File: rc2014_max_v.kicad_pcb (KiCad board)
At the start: 2 copper layers, 101.6 x 50.8 mm, 105 parts, among them J1 M3 Mounting Hole, J2 Conn_01x40, J3 Pro Bus, J4 Conn_01x24, J5 AVR-JTAG-10, J6 USB_B_Micro, J7 PMOD, J8 PMOD, SW1 SW_Push, SW2 SW_Push, U1 MIC5356-SGYMME, U10 93LCxxBxxOT, U11 5M570ZT100I5N, U12 IS61LV5128AL-10TLI, U2 SN74ALVC164245DGG, U3 SN74ALVC164245DGG, U4 TXB0108PWR, U5 TXB0108PWR, U6 SN74ALVC164245DGG, U7 MIC5356-SGYMME, U8 TPD2EUSB30, U9 FT2232H, X1 CB3LV-3I-50M0000, Y1 CTS-445 12Mhz

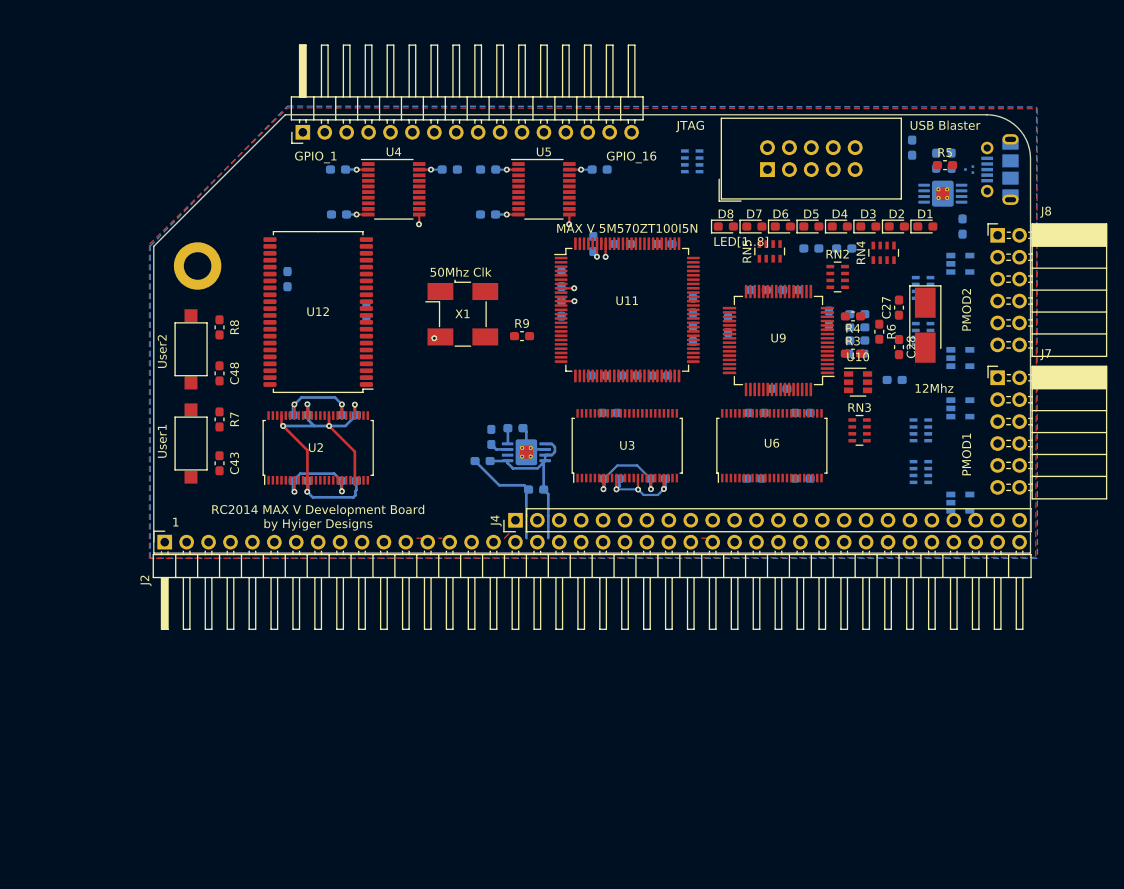
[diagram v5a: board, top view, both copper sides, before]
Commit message: Added logo, cpio vcc selection
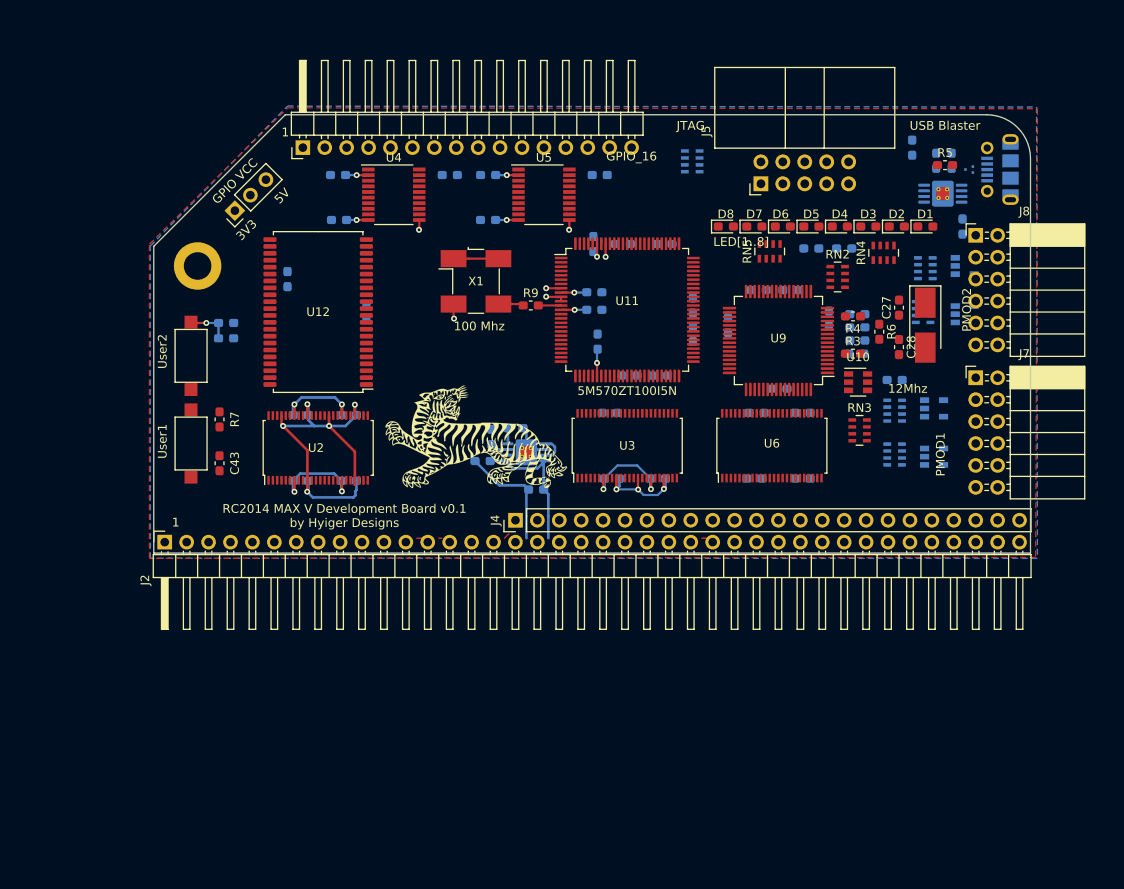
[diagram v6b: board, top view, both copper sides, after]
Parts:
- added G***: LOGO, Logos:asian_tiger, F.Cu at (112.8, 114.0)
- added JP1: Jumper_3_Bridged12, Connector_PinHeader_2.54mm:PinHeader_1x03_P2.54mm_Vertical, F.Cu at (84.8, 87.8)
- C48, R8: moved to B.Cu
- J5: footprint Connector_IDC:IDC-Header_2x05_P2.54mm_Vertical -> Connector_IDC:IDC-Header_2x05_P2.54mm_Horizontal
- moved D11 6.14 mm to (165.9, 116.3)
- moved C48 5.89 mm to (83.8, 100.8), turned to 0 degrees
- moved D9 5.11 mm to (169.4, 99.8)
- moved C41 4.10 mm to (126.5, 97.3), turned to 0 degrees
- moved X1 4.10 mm to (112.8, 96.0)
- moved C40 3.94 mm to (126.9, 103.0), turned to 90 degrees
- moved C47 3.81 mm to (126.5, 99.3), turned to 0 degrees
- moved RN9 3.81 mm to (161.3, 111.0)
- moved R9 3.70 mm to (119.1, 98.8)
- moved RN8 3.66 mm to (161.3, 116.1)
- moved D12 3.05 mm to (165.9, 110.7)
- moved J7 2.54 mm to (170.7, 107.2)
- moved J8 2.54 mm to (170.7, 90.7)
- moved RN6 2.54 mm to (164.6, 99.6)
- moved RN7 2.30 mm to (164.8, 94.5)
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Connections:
- C16 pad 1: 5V -> VCC_GPIO
- C17 pad 1: 5V -> VCC_GPIO
- D1 pad 1: LED1 -> (no net)
- D2 pad 1: LED2 -> (no net)
- D3 pad 1: LED3 -> (no net)
- D4 pad 1: LED4 -> (no net)
- D5 pad 1: LED5 -> (no net)
- D6 pad 1: LED6 -> (no net)
- D7 pad 1: LED7 -> (no net)
- D8 pad 1: LED8 -> (no net)
- J2 pad 35: TX_A -> (no net)
- J2 pad 37: Net-(J2-Pad37) -> (no net)
- J2 pad 38: Net-(J2-Pad38) -> (no net)
- J2 pad 39: Net-(J2-Pad39) -> (no net)
- J2 pad 40: Net-(J2-Pad40) -> (no net)
- J4 pad 19: TX_B -> (no net)
- J4 pad 20: RX_B -> (no net)
- J4 pad 21: Net-(J4-Pad21) -> (no net)
- J4 pad 22: Net-(J4-Pad22) -> (no net)
- J4 pad 23: Net-(J4-Pad23) -> (no net)
- J4 pad 24: Net-(J4-Pad24) -> (no net)
- J4 pad 3: ~RFSH -> (no net)
- J4 pad 5: CLK2 -> (no net)
- J5 pad 4: Net-(J5-Pad4) -> +3V3
- J5 pad 6: Net-(J5-Pad6) -> +3V3
- J5 pad 7: Net-(J5-Pad7) -> (no net)
- J5 pad 8: Net-(J5-Pad8) -> (no net)
- RN1 pad 8: +3V3 -> GND
- RN3 pad 4: Net-(RN3-Pad4) -> (no net)
- U1 pad 6: Net-(U1-Pad6) -> (no net)
- U11 pad 22: Net-(U11-Pad22) -> (no net)
- U11 pad 23: Net-(U11-Pad23) -> (no net)
- U11 pad 24: Net-(U11-Pad24) -> (no net)
- U11 pad 25: Net-(U11-Pad25) -> (no net)
- U11 pad 41: ~M1_F -> D0_F
- U11 pad 42: ~MREQ_F -> D1_F
- U11 pad 43: ~WR_F -> D2_F
- U11 pad 44: ~RD_F -> D3_F
- U11 pad 47: ~IORQ_F -> D4_F
- U11 pad 48: ~PAGE_F -> D5_F
- U11 pad 49: ~BUSACK_F -> D6_F
- U11 pad 50: Net-(U11-Pad50) -> D7_F
- U11 pad 51: Net-(U11-Pad51) -> (no net)
- U11 pad 61: Net-(U11-Pad61) -> ~BUSACK_F
- U11 pad 62: Net-(U11-Pad62) -> ~PAGE_F
- U11 pad 64: Net-(U11-Pad64) -> ~IORQ_F
- U11 pad 66: Net-(U11-Pad66) -> ~RD_F
- U11 pad 67: RX_A_F -> ~WR_F
- U11 pad 68: Net-(U11-Pad68) -> ~MREQ_F
- U11 pad 69: Net-(U11-Pad69) -> ~M1_F
- U11 pad 70: Net-(U11-Pad70) -> (no net)
- U11 pad 71: Net-(U11-Pad71) -> (no net)
- U11 pad 72: Net-(U11-Pad72) -> (no net)
- U11 pad 73: Net-(U11-Pad73) -> (no net)
- U11 pad 74: Net-(U11-Pad74) -> (no net)
- U11 pad 75: Net-(U11-Pad75) -> (no net)
- U11 pad 76: Net-(U11-Pad76) -> (no net)
- U11 pad 77: Net-(U11-Pad77) -> (no net)
- U11 pad 78: Net-(U11-Pad78) -> (no net)
- U12 pad 1: Net-(U12-Pad1) -> (no net)
- U12 pad 15: Net-(U12-Pad15) -> (no net)
- U12 pad 2: Net-(U12-Pad2) -> (no net)
- U12 pad 21: Net-(U12-Pad21) -> (no net)
- U12 pad 22: Net-(U12-Pad22) -> (no net)
- U12 pad 23: Net-(U12-Pad23) -> (no net)
- U12 pad 24: Net-(U12-Pad24) -> (no net)
- U12 pad 25: Net-(U12-Pad25) -> (no net)
- U12 pad 37: Net-(U12-Pad37) -> (no net)
- U12 pad 39: Net-(U12-Pad39) -> (no net)
- U12 pad 40: Net-(U12-Pad40) -> (no net)
- U12 pad 41: Net-(U12-Pad41) -> (no net)
- U12 pad 42: Net-(U12-Pad42) -> (no net)
- U12 pad 43: Net-(U12-Pad43) -> (no net)
- U12 pad 44: Net-(U12-Pad44) -> (no net)
- U12 pad 8: Net-(U12-Pad8) -> (no net)
- U3 pad 25: OE_C_I -> (no net)
- U3 pad 37: RX_A_F -> (no net)
- U3 pad 48: OE_C_O -> (no net)
- U3 pad 5: ~RESET2 -> (no net)
- U4 pad 1: Net-(U4-Pad1) -> (no net)
- U4 pad 19: 5V -> VCC_GPIO
- U4 pad 3: Net-(U4-Pad3) -> (no net)
- U4 pad 4: Net-(U4-Pad4) -> (no net)
- U4 pad 5: Net-(U4-Pad5) -> (no net)
- U4 pad 6: Net-(U4-Pad6) -> (no net)
- U4 pad 7: Net-(U4-Pad7) -> (no net)
- U4 pad 8: Net-(U4-Pad8) -> (no net)
- U4 pad 9: Net-(U4-Pad9) -> (no net)
- U5 pad 1: Net-(U5-Pad1) -> (no net)
- U5 pad 19: 5V -> VCC_GPIO
- U5 pad 3: Net-(U5-Pad3) -> (no net)
- U5 pad 4: Net-(U5-Pad4) -> (no net)
- U5 pad 5: Net-(U5-Pad5) -> (no net)
- U5 pad 6: Net-(U5-Pad6) -> (no net)
- U5 pad 7: Net-(U5-Pad7) -> (no net)
- U5 pad 8: Net-(U5-Pad8) -> (no net)
- U5 pad 9: Net-(U5-Pad9) -> (no net)
- U6 pad 26: D15_F -> (no net)
- U6 pad 29: D14_F -> (no net)
- U6 pad 32: D13_F -> (no net)
- U6 pad 35: D12_F -> (no net)
- U6 pad 37: D11_F -> (no net)
- U6 pad 40: D10_F -> (no net)
- U6 pad 43: D9_F -> (no net)
- U6 pad 46: D8_F -> (no net)
- U7 pad 6: Net-(U7-Pad6) -> (no net)
- U9 pad 21: Net-(U9-Pad21) -> (no net)
- U9 pad 22: Net-(U9-Pad22) -> (no net)
- U9 pad 23: Net-(U9-Pad23) -> (no net)
- U9 pad 24: Net-(U9-Pad24) -> (no net)
- U9 pad 26: Net-(U9-Pad26) -> (no net)
- U9 pad 27: Net-(U9-Pad27) -> (no net)
- U9 pad 28: Net-(U9-Pad28) -> (no net)
- U9 pad 29: Net-(U9-Pad29) -> (no net)
- U9 pad 30: Net-(U9-Pad30) -> (no net)
- U9 pad 32: Net-(U9-Pad32) -> (no net)
- U9 pad 33: Net-(U9-Pad33) -> (no net)
- U9 pad 34: Net-(U9-Pad34) -> (no net)
- U9 pad 36: Net-(U9-Pad36) -> (no net)
- U9 pad 38: Net-(U9-Pad38) -> (no net)
- U9 pad 39: Net-(U9-Pad39) -> (no net)
- U9 pad 40: Net-(U9-Pad40) -> (no net)
- U9 pad 41: Net-(U9-Pad41) -> (no net)
- U9 pad 43: Net-(U9-Pad43) -> (no net)
- U9 pad 44: Net-(U9-Pad44) -> (no net)
- U9 pad 45: Net-(U9-Pad45) -> (no net)
- U9 pad 46: Net-(U9-Pad46) -> (no net)
- U9 pad 48: Net-(U9-Pad48) -> (no net)
- U9 pad 49: Net-(U9-Pad49) -> (no net)
- U9 pad 50: Net-(U9-Pad50) -> (no net)
- U9 pad 52: Net-(U9-Pad52) -> (no net)
- U9 pad 53: Net-(U9-Pad53) -> (no net)
- U9 pad 54: Net-(U9-Pad54) -> (no net)
- U9 pad 55: Net-(U9-Pad55) -> (no net)
- U9 pad 57: Net-(U9-Pad57) -> (no net)
- U9 pad 58: Net-(U9-Pad58) -> (no net)
- U9 pad 59: Net-(U9-Pad59) -> (no net)
- U9 pad 60: Net-(U9-Pad60) -> (no net)
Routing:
- net +3V3: track 19.2 -> 30.5 mm, vias 4 -> 6
- net 5V: track 49.2 -> 43.9 mm, vias 6 -> 4
- net SW_USER2: track 0.00 -> 5.00 mm, vias 0 -> 1
- net +1V8: track 2.13 -> 5.11 mm, vias 0 -> 1
- net Net-(R9-Pad1): track 0.00 -> 2.94 mm
- net IO1_CLK0: track 0.00 -> 2.64 mm
- net GND: track 87.0 -> 88.4 mm
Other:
- board text added: "100 Mhz"
- board text added: "3V3"
- board text added: "5M570ZT100I5N"
- board text added: "5V"
- board text added: "GPIO VCC"
- board text added: "RC2014 MAX V Development Board v0.1 by Hyiger Designs"
- board text removed: "50Mhz Clk"
- board text removed: "GPIO_1"
- board text removed: "MAX V 5M570ZT100I5N"
- board text removed: "RC2014 MAX V Development Board by Hyiger Designs"

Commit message: larger maxv, additional clocks, reorganized sheets
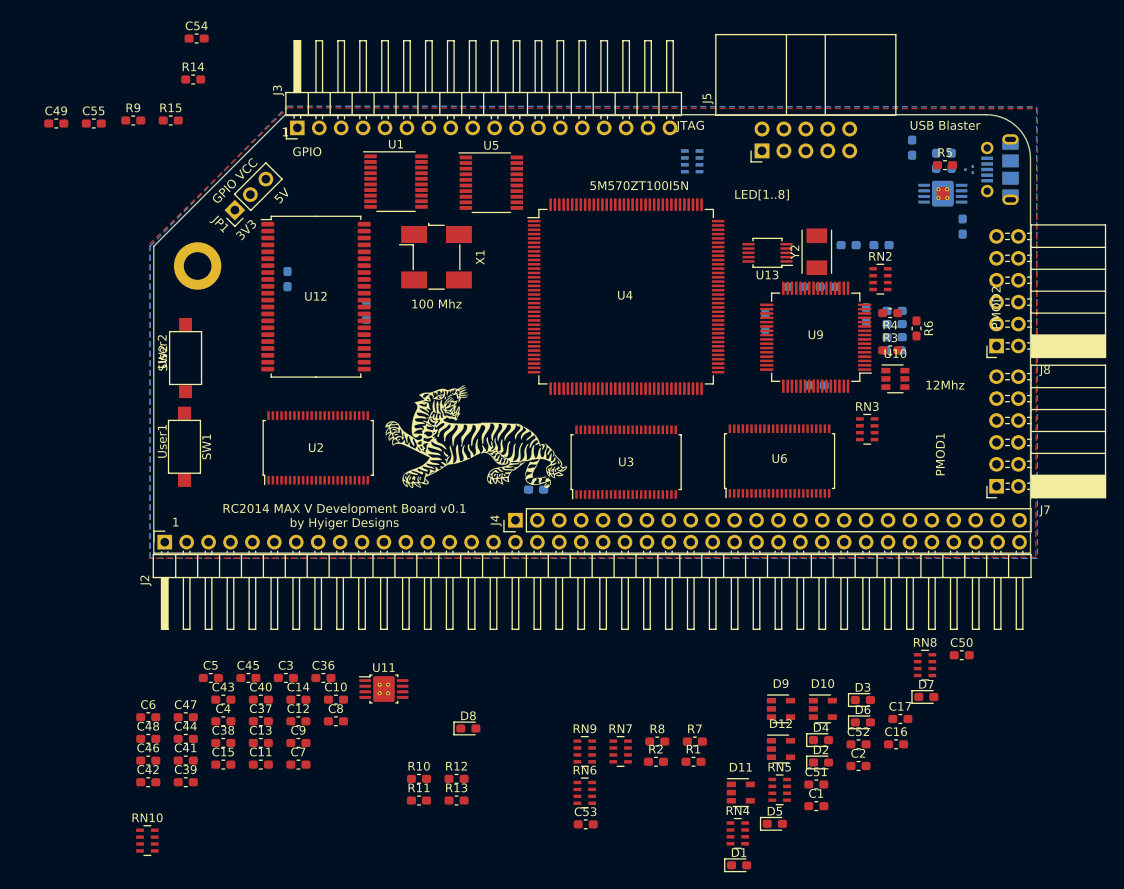
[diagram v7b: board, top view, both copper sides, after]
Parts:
- removed C27, C28: 18pF, Capacitor_SMD:C_0603_1608Metric_Pad1.05x0.95mm_HandSolder
- removed Y1: CTS-445 12Mhz, Crystal:Crystal_SMD_5032-2Pin_5.0x3.2mm_HandSoldering
- added C50: 100nF, Capacitor_SMD:C_0603_1608Metric_Pad1.05x0.95mm_HandSolder, F.Cu at (169.1, 139.3)
- added C51: 100nF, Capacitor_SMD:C_0603_1608Metric_Pad1.05x0.95mm_HandSolder, F.Cu at (152.2, 154.3)
- added C52: 100nF, Capacitor_SMD:C_0603_1608Metric_Pad1.05x0.95mm_HandSolder, F.Cu at (157.1, 149.7)
- added C53: 100nF, Capacitor_SMD:C_0603_1608Metric_Pad1.05x0.95mm_HandSolder, F.Cu at (125.5, 158.9)
- added C54: 0.47uF, Capacitor_SMD:C_0603_1608Metric_Pad1.05x0.95mm_HandSolder, F.Cu at (80.4, 67.9)
- added C55: 0.47uF, Capacitor_SMD:C_0603_1608Metric_Pad1.05x0.95mm_HandSolder, F.Cu at (68.5, 77.7)
- added R10: 10K, Resistor_SMD:R_0603_1608Metric_Pad1.05x0.95mm_HandSolder, F.Cu at (106.2, 153.7)
- added R11: 10K, Resistor_SMD:R_0603_1608Metric_Pad1.05x0.95mm_HandSolder, F.Cu at (106.2, 156.2)
- added R12: 10K, Resistor_SMD:R_0603_1608Metric_Pad1.05x0.95mm_HandSolder, F.Cu at (110.5, 153.7)
- added R13: 10K, Resistor_SMD:R_0603_1608Metric_Pad1.05x0.95mm_HandSolder, F.Cu at (110.5, 156.2)
- added R14: 1K, Resistor_SMD:R_0603_1608Metric_Pad1.05x0.95mm_HandSolder, F.Cu at (80.0, 72.6)
- added R15: 1K, Resistor_SMD:R_0603_1608Metric_Pad1.05x0.95mm_HandSolder, F.Cu at (77.4, 77.4)
- added RN10: 10K, Resistor_SMD:R_Array_Concave_4x0603, F.Cu at (74.7, 160.8)
- added U13: Si5351A-B-GT, Package_SO:MSOP-10_3x3mm_P0.5mm, F.Cu at (146.6, 92.7)
- added Y2: 25MHZ 8PF, Crystal:Crystal_SMD_TXC_7A-2Pin_5x3.2mm, F.Cu at (152.3, 92.6)
- C1, C10, C11, C12, C13, C14, C15, C16, C17, C2, C3, C36, C37, C38, C39, C4, C40, C41, C42, C44, C45, C46, C47, C48, C49, C5, C6, C7, C9, D10, D11, D12, D9, R8, RN6, RN7, RN8, RN9: moved to F.Cu
- C43: value 100nF -> 2.2uF
- C8: value 2.2uF -> 100nF; moved to F.Cu
- J3: footprint Connector_PinHeader_2.54mm:PinHeader_1x16_P2.54mm_Horizontal -> Connector_PinHeader_2.54mm:PinHeader_1x18_P2.54mm_Horizontal
- J7: value PMOD -> PMOD1
- R1, R2: value 50K -> 1K; moved to F.Cu
- U1: value MIC5356-SGYMME -> TXB0108PWR; footprint Package_SO:MSOP-8-1EP_3x3mm_P0.65mm_EP2.5x3mm_Mask1.73x2.36mm_ThermalVias -> Package_SO:TSSOP-20_4.4x6.5mm_P0.65mm; moved to F.Cu
- U11: value 5M570ZT100I5N -> MIC5356-SGYMME; footprint Package_QFP:TQFP-100_14x14mm_P0.5mm -> Package_SO:MSOP-8-1EP_3x3mm_P0.65mm_EP2.5x3mm_Mask1.73x2.36mm_ThermalVias
- U4: value TXB0108PWR -> 5M1270ZT144C5N; footprint Package_SO:TSSOP-20_4.4x6.5mm_P0.65mm -> Package_QFP:TQFP-144_20x20mm_P0.5mm
- moved C6 94.9 mm to (74.8, 146.5), turned to 0 degrees
- moved C49 92.8 mm to (64.1, 77.7)
- moved C16 83.8 mm to (161.5, 149.7)
- moved D1 77.1 mm to (143.3, 163.7)
- moved C44 76.5 mm to (79.1, 149.0), turned to 0 degrees
- moved R1 75.0 mm to (138.0, 151.7), turned to 0 degrees
- moved C1 75.0 mm to (152.2, 156.8)
- moved C42 73.7 mm to (74.8, 154.1), turned to 0 degrees
- moved C37 72.4 mm to (87.8, 147.0)
- moved C39 72.4 mm to (79.1, 154.1)
- moved C38 72.2 mm to (83.5, 149.5), turned to 0 degrees
- moved C17 72.0 mm to (162.0, 146.7)
- moved C41 72.0 mm to (79.1, 151.5)
- moved C2 71.7 mm to (157.1, 152.2)
- moved C46 71.4 mm to (74.8, 151.5), turned to 0 degrees
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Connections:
- net OE_D renamed OE_D1
- C1 pad 1: +3V3 -> SW_USER1
- C15 pad 1: 5V -> +1V8
- C2 pad 1: +3V3 -> SW_USER2
- C43 pad 1: SW_USER1 -> 5V
- C48 pad 1: SW_USER2 -> +3V3
- C7 pad 1: +1V8 -> +3V3
- C8 pad 1: 5V -> +3V3
- C9 pad 1: +3V3 -> 5V
- D1 pad 1: (no net) -> LED1
- D2 pad 1: (no net) -> LED2
- D3 pad 1: (no net) -> LED3
- D4 pad 1: (no net) -> LED4
- D5 pad 1: (no net) -> LED5
- D6 pad 1: (no net) -> LED6
- D7 pad 1: (no net) -> LED7
- D8 pad 1: (no net) -> LED8
- J3 pad 1: GPIO_1 -> GND
- J3 pad 10: GPIO_10 -> GPIO_8
- J3 pad 11: GPIO_11 -> GPIO_9
- J3 pad 12: GPIO_12 -> GPIO_10
- J3 pad 13: GPIO_13 -> GPIO_11
- J3 pad 14: GPIO_14 -> GPIO_12
- J3 pad 15: GPIO_15 -> GPIO_13
- J3 pad 16: GPIO_16 -> GPIO_14
- J3 pad 2: GPIO_2 -> VCC_GPIO
- J3 pad 3: GPIO_3 -> GPIO_1
- J3 pad 4: GPIO_4 -> GPIO_2
- J3 pad 5: GPIO_5 -> GPIO_3
- J3 pad 6: GPIO_6 -> GPIO_4
- J3 pad 7: GPIO_7 -> GPIO_5
- J3 pad 8: GPIO_8 -> GPIO_6
- J3 pad 9: GPIO_9 -> GPIO_7
- RN6 pad 5: GPIO_4 -> PMOD1_4
- RN6 pad 6: GPIO_3 -> PMOD1_3
- RN6 pad 7: GPIO_2 -> PMOD1_2
- RN6 pad 8: GPIO_1 -> PMOD1_1
- RN7 pad 5: GPIO_8 -> PMOD1_5
- RN7 pad 6: GPIO_7 -> PMOD1_6
- RN7 pad 7: GPIO_6 -> PMOD1_7
- RN7 pad 8: GPIO_5 -> PMOD1_8
- RN8 pad 5: GPIO_13 -> PMOD2_4
- RN8 pad 6: GPIO_12 -> PMOD2_3
- RN8 pad 7: GPIO_11 -> PMOD2_2
- RN8 pad 8: GPIO_10 -> PMOD2_1
- RN9 pad 5: GPIO_16 -> PMOD2_5
- RN9 pad 6: GPIO_15 -> PMOD2_6
- RN9 pad 7: GPIO_14 -> PMOD2_7
- RN9 pad 8: GPIO_13 -> PMOD2_8
- U1 pad 1: 5V -> GPIO_1_F
- U1 pad 2: GND -> +3V3
- U1 pad 3: 5V -> GPIO_2_F
- U1 pad 4: 5V -> GPIO_3_F
- U1 pad 5: 5V -> GPIO_4_F
- U1 pad 6: (no net) -> GPIO_5_F
- U1 pad 7: +1V8 -> GPIO_6_F
- U1 pad 8: +3V3 -> GPIO_7_F
- U1 pad 9: GND -> GPIO_8_F
- U11 pad 1: GPIO_16 -> 5V
- U11 pad 2: A10_F -> GND
- U11 pad 3: A11_F -> 5V
- U11 pad 4: A12_F -> 5V
- U11 pad 5: A13_F -> 5V
- U11 pad 6: A14_F -> (no net)
- U11 pad 7: A15_F -> +1V8
- U11 pad 8: GND -> +3V3
- U11 pad 9: +3V3 -> GND
- U12 pad 15: (no net) -> ~OE~_RAM
- U12 pad 37: (no net) -> ~WE~_RAM
- U12 pad 8: (no net) -> ~CE~_RAM
- U3 pad 1: ~DIR -> (no net)
- U3 pad 24: DIR -> (no net)
- U3 pad 25: (no net) -> OE_C_I
- U3 pad 48: (no net) -> OE_C_O
- U4 pad 1: (no net) -> ~WE~_RAM
- U4 pad 10: OE_G_1 -> GND
- U4 pad 12: GPIO_8 -> A13_F
- U4 pad 13: GPIO_7 -> A14_F
- U4 pad 14: GPIO_6 -> A15_F
- U4 pad 15: GPIO_5 -> A4_F
- U4 pad 16: GPIO_4 -> A5_F
- U4 pad 17: GPIO_3 -> GND
- U4 pad 18: GPIO_2 -> CLK_50Mhz
- U4 pad 19: VCC_GPIO -> +1V8
- U4 pad 2: +3V3 -> ~OE~_RAM
- U4 pad 20: GPIO_1 -> CLK_7_3728_Mhz
- U4 pad 3: (no net) -> ~CE~_RAM
- U4 pad 6: (no net) -> A10_F
- U4 pad 7: (no net) -> A11_F
- U4 pad 8: (no net) -> A12_F
- U4 pad 9: (no net) -> +3V3
- U5 pad 1: (no net) -> GPIO_9_F
- U5 pad 3: (no net) -> GPIO_10_F
- U5 pad 4: (no net) -> GPIO_11_F
- U5 pad 5: (no net) -> GPIO_12_F
- U5 pad 6: (no net) -> GPIO_13_F
- U5 pad 7: (no net) -> GPIO_14_F
- U5 pad 8: (no net) -> GPIO_15_F
- U5 pad 9: (no net) -> GPIO_16_F
- U6 pad 1: ~DIR -> DIR_D
- U6 pad 24: ~DIR -> DIR_D
- U6 pad 26: (no net) -> D15_F
- U6 pad 29: (no net) -> D14_F
- U6 pad 32: (no net) -> D13_F
- U6 pad 35: (no net) -> D12_F
- U6 pad 37: (no net) -> D11_F
- U6 pad 40: (no net) -> D10_F
- U6 pad 43: (no net) -> D9_F
- U6 pad 46: (no net) -> D8_F
- U9 pad 2: Net-(C27-Pad1) -> CLK_12Mhz
- U9 pad 3: Net-(C28-Pad1) -> (no net)
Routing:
- net GND: track 88.4 -> 0.00 mm, vias 15 -> 0
- net 5V: track 43.9 -> 0.00 mm, vias 4 -> 0
- net +3V3: track 30.5 -> 0.00 mm, vias 6 -> 0
- net +1V8: track 5.11 -> 0.00 mm, vias 1 -> 0
- net SW_USER2: track 5.00 -> 0.00 mm, vias 1 -> 0
- net Net-(R9-Pad1): track 2.94 -> 0.00 mm
- net OE_G_2: track 2.65 -> 0.00 mm, vias 1 -> 0
- net IO1_CLK0: track 2.64 -> 0.00 mm
- net OE_G_1: track 2.53 -> 0.00 mm, vias 1 -> 0
- net A0: track 1.20 -> 0.00 mm
- net A3: track 1.09 -> 0.00 mm
- net ~IORQ: track 0.71 -> 0.00 mm
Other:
- board text added: "GPIO"
- board text removed: "GPIO_16"
